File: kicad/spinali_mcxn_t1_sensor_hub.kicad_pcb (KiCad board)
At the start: 6 copper layers, 36.6 x 46 mm, 204 parts, among them J1 5055780421, J10 SDO, J11 CKO, J12 GND, J2 USB4105-GF-A, J3 CAN0A, J4 CAN0B, J5 Debug, J6 CAN1A, J7 CAN1B, J8 DF40TC(3.0)-50DP-0.4V(51), J9 DF40TC(3.0)-50DP-0.4V(51), Q1 BUK6D56-60EX, SW1 SW_SPST, U1 LM74700, U10 BMM350, U11 BMP581, U12 TJA1462ATK, U13 TJA1462ATK, U14 SK9822-EC20, U15 TJA1103AHN, U2 NX5P3363UKZ, U3 LM5160DNTJ, U4 NX5P3363UKZ, U5 MIC5504-1.8YMT, U6 MPM3811GG-Z, U7 MCXN947VDFT, U8 PCMF1USB3SZ, U9 ICM-45686, Y1 24MHz, Y2 32.768kHz, Y3 25MHz

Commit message: Updated layout
Added formal board-name in silkscreen.
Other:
- board text added: "X-MR-MCXN-T1"
- board text removed: "MR-XXX-XXX"
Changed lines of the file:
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@@
 		)
 	)
-	(gr_text "MR-XXX-XXX"
+	(gr_text "X-MR-MCXN-T1"
 		(at 118.2 100.5 90)
 		(layer "B.SilkS")

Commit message: Updated layout
Made edge cut dimensions easy to work with values.
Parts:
- moved J2 0.06 mm to (85.9, 100.7)
- moved U8 0.05 mm to (91.4, 100.2)
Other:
- board size 36.6 x 46 mm -> 36.5 x 46 mm
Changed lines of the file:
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@@
 	(footprint "TVS:PESD1USB3BCX"
 		(layer "B.Cu")
-		(at 91.35 100.2 -90)
+		(at 91.4 100.2 -90)
 		(descr "WLCSP5_2-1-2")
 		(tags "Diode")
@@
 	(footprint "Connector_USB:USB_C_Receptacle_GCT_USB4105-xx-A_16P_TopMnt_Horizontal"
 		(layer "B.Cu")
-		(at 85.85 100.7 90)
+		(at 85.91 100.7 90)
 		(descr "USB 2.0 Type C Receptacle, GCT, 16P, top mounted, horizontal, 5A: https://gct.co/files/drawings/usb4105.pdf")
 		(tags "USB C Type-C Receptacle SMD USB 2.0 16P 16C USB4105-15-A USB4105-15-A-060 USB4105-15-A-120 USB4105-GF-A USB4105-GF-A-060 USB4105-GF-A-120")
@@
 	)
 	(gr_rect
-		(start 82.15 75.95)
-		(end 118.75 122)
+		(start 82.2 75.95)
+		(end 118.7 121.95)
 		(stroke
 			(width 0.05)
@@
 	)
 	(via
-		(at 91.35 99.8)
+		(at 91.4 99.8)
 		(size 0.3)
 		(drill 0.2)
@@
 	)
 	(via
-		(at 91.35 100.6)
+		(at 91.4 100.6)
 		(size 0.3)
 		(drill 0.2)
@@
 	)
 	(segment
-		(start 91.35 100.2)
-		(end 91.35 99.85)
+		(start 91.4 100.2)
+		(end 91.4 99.85)
 		(width 0.16)
 		(layer "B.Cu")
@@
 	)
 	(segment
-		(start 91.35 99.85)
-		(end 91.35 99.8)
+		(start 91.4 99.85)
+		(end 91.4 99.8)
 		(width 0.16)
 		(layer "B.Cu")
@@
 	)
 	(segment
-		(start 91.35 100.55)
-		(end 91.35 100.6)
+		(start 91.4 100.55)
+		(end 91.4 100.6)
 		(width 0.16)
 		(layer "B.Cu")
@@
 	)
 	(segment
-		(start 91.35 100.2)
-		(end 91.35 100.55)
+		(start 91.4 100.2)
+		(end 91.4 100.55)
 		(width 0.16)
 		(layer "B.Cu")
@@
 	)
 	(segment
-		(start 88.55 102.730406)
-		(end 88.922297 103.102703)
+		(start 89.59 98.3)
+		(end 88.979594 98.3)
 		(width 0.3)
 		(layer "B.Cu")
@@
 	)
 	(segment
-		(start 89.527297 103.102703)
-		(end 89.53 103.1)
-		(width 0.3)
+		(start 88.025 102.205406)
+		(end 88.025 99.230001)
+		(width 0.5)
 		(layer "B.Cu")
 		(net 22)
 	)
 	(segment
-		(start 88.955001 98.3)
-		(end 88.630001 98.625)
+		(start 88.979594 103.1)
+		(end 89.53 103.1)
 		(width 0.3)
 		(layer "B.Cu")
@@
 	)
 	(segment
-		(start 88.922297 103.102703)
-		(end 89.527297 103.102703)
+		(start 88.61 102.730406)
+		(end 88.979594 103.1)
 		(width 0.3)
 		(layer "B.Cu")
@@
 	)
 	(segment
-		(start 89.53 98.3)
+		(start 89.59 98.3)
 		(end 90.4 98.3)
 		(width 0.5)
@@
 	)
 	(segment
-		(start 88.025 102.205406)
-		(end 88.025 99.230001)
+		(start 88.55 102.730406)
+		(end 88.61 102.730406)
+		(width 0.3)
+		(layer "B.Cu")
+		(net 22)
+	)
+	(segment
+		(start 88.025 99.230001)
+		(end 88.630001 98.625)
 		(width 0.5)
 		(layer "B.Cu")
@@
 	)
 	(segment
-		(start 88.025 99.230001)
+		(start 88.654594 98.625)
 		(end 88.630001 98.625)
-		(width 0.5)
+		(width 0.3)
 		(layer "B.Cu")
 		(net 22)
 	)
 	(segment
-		(start 89.53 98.3)
-		(end 88.955001 98.3)
+		(start 88.979594 98.3)
+		(end 88.654594 98.625)
 		(width 0.3)
 		(layer "B.Cu")
@@
 	)
 	(segment
-		(start 87.67 96.38)
-		(end 88.955 96.38)
-		(width 0.1)
-		(layer "F.Cu")
-		(net 24)
-	)
-	(segment
-		(start 83.605 105.02)
-		(end 83.6 105.025)
-		(width 0.1)
-		(layer "F.Cu")
-		(net 24)
-	)
-	(segment
 		(start 83.47 101.175)
 		(end 83.47 100.695)
@@
 	)
 	(segment
-		(start 84.775 105.02)
-		(end 83.605 105.02)
+		(start 87.7 96.38)
+		(end 88.955 96.38)
 		(width 0.1)
 		(layer "F.Cu")
@@
 	)
 	(segment
-		(start 87.65 96.4)
-		(end 87.67 96.38)
+		(start 83.47 100.695)
+		(end 83.45 100.675)
 		(width 0.1)
 		(layer "F.Cu")
@@
 	)
 	(segment
-		(start 83.47 100.695)
+		(start 83.44 100.665)
 		(end 83.45 100.675)
 		(width 0.1)
@@
 	)
 	(segment
-		(start 83.44 100.665)
-		(end 83.45 100.675)
+		(start 83.7 96.38)
+		(end 84.775 96.38)
 		(width 0.1)
 		(layer "F.Cu")
@@
 	)
 	(segment
-		(start 83.62 96.38)
-		(end 84.775 96.38)
+		(start 83.65 105.02)
+		(end 84.775 105.02)
 		(width 0.1)
 		(layer "F.Cu")
@@
 	)
 	(segment
-		(start 87.63 105.02)
+		(start 87.7 105.02)
 		(end 88.955 105.02)
 		(width 0.1)
@@
 	)
 	(via
-		(at 83.62 96.38)
+		(at 83.7 96.38)
 		(size 0.3)
 		(drill 0.2)
@@
 	)
 	(via
-		(at 87.63 105.02)
+		(at 87.7 105.02)
 		(size 0.3)
 		(drill 0.2)
@@
 	)
 	(via
-		(at 83.6 105.025)
+		(at 83.65 105.02)
 		(size 0.3)
 		(drill 0.2)
@@
 	)
 	(via
-		(at 87.65 96.4)
+		(at 87.7 96.38)
 		(size 0.3)
 		(drill 0.2)
@@
 	)
 	(segment
-		(start 89.53 100.95)
-		(end 88.89 100.95)
-		(width 0.16)
-		(layer "B.Cu")
-		(net 231)
-	)
-	(segment
-		(start 89.53 99.95)
-		(end 89.58 100)
+		(start 88.63 100.21)
+		(end 88.89 99.95)
 		(width 0.16)
 		(layer "B.Cu")
@@
 	)
 	(segment
-		(start 88.63 100.69)
-		(end 88.63 100.21)
+		(start 89.53 100.95)
+		(end 88.89 100.95)
 		(width 0.16)
 		(layer "B.Cu")
@@
 	)
 	(segment
-		(start 88.63 100.21)
-		(end 88.89 99.95)
+		(start 89.58 100)
+		(end 91 100)
 		(width 0.16)
 		(layer "B.Cu")
@@
 	)
 	(segment
-		(start 88.89 99.95)
-		(end 89.53 99.95)
+		(start 88.63 100.69)
+		(end 88.63 100.21)
 		(width 0.16)
 		(layer "B.Cu")
@@
 	)
 	(segment
-		(start 89.58 100)
-		(end 90.95 100)
+		(start 89.53 99.95)
+		(end 89.58 100)
 		(width 0.16)
 		(layer "B.Cu")
@@
 	)
 	(segment
-		(start 90.17 101.45)
-		(end 90.44 101.18)
-		(width 0.16)
-		(layer "B.Cu")
-		(net 232)
-	)
-	(segment
-		(start 90.44 101.18)
-		(end 90.44 100.41)
+		(start 88.89 99.95)
+		(end 89.53 99.95)
 		(width 0.16)
 		(layer "B.Cu")
-		(net 232)
+		(net 231)
 	)
 	(segment
-		(start 90.36 100.41)
-		(end 90.916532 100.41)
+		(start 89.53 100.45)
+		(end 89.57 100.41)
 		(width 0.16)
 		(layer "B.Cu")
@@
 	)
 	(segment
-		(start 89.57 100.41)
-		(end 90.36 100.41)
+		(start 90.17 101.45)
+		(end 90.44 101.18)
 		(width 0.16)
 		(layer "B.Cu")
@@
 	)
 	(segment
-		(start 90.916532 100.41)
-		(end 90.928266 100.421734)
+		(start 89.57 100.41)
+		(end 90.99 100.41)
 		(width 0.16)
 		(layer "B.Cu")
@@
 	)
 	(segment
-		(start 89.53 100.45)
-		(end 89.57 100.41)
+		(start 90.44 101.18)
+		(end 90.44 100.41)
 		(width 0.16)
 		(layer "B.Cu")
@@
 	)
 	(segment
-		(start 92.45 100.4)
-		(end 91.75 100.4)
+		(start 92.6 100.55)
+		(end 92.45 100.4)
 		(width 0.16)
 		(layer "B.Cu")
@@
 	)
 	(segment
-		(start 92.6 100.55)
-		(end 92.45 100.4)
+		(start 92.45 100.4)
+		(end 91.8 100.4)
 		(width 0.16)
 		(layer "B.Cu")
@@
 	(segment
 		(start 92.6764 99.99)
-		(end 91.76 99.99)
+		(end 91.81 99.99)
 		(width 0.16)
 		(layer "B.Cu")
@@
 	)
 	(segment
-		(start 92.9182 100.2318)
-		(end 92.6764 99.99)
+		(start 91.81 99.99)
+		(end 91.8 100)
 		(width 0.16)
 		(layer "B.Cu")
@@
 	)
 	(segment
-		(start 91.76 99.99)
-		(end 91.75 100)
+		(start 92.9182 100.2318)
+		(end 92.6764 99.99)
 		(width 0.16)
 		(layer "B.Cu")

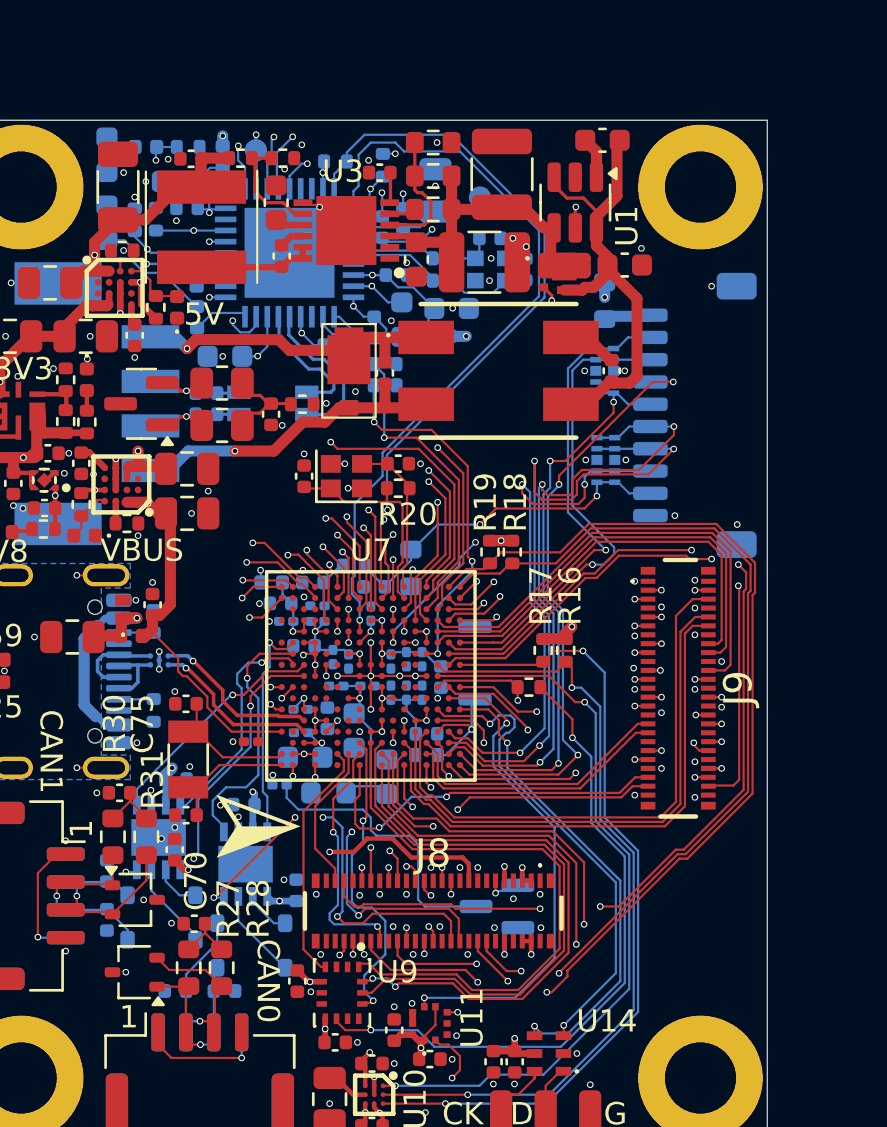
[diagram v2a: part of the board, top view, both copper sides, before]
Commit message: Update layout
- Length matched MII RX and TX.
- Made clearance between USB D+ and D- traces constant.
- Improved traces for 32kHz crystal.
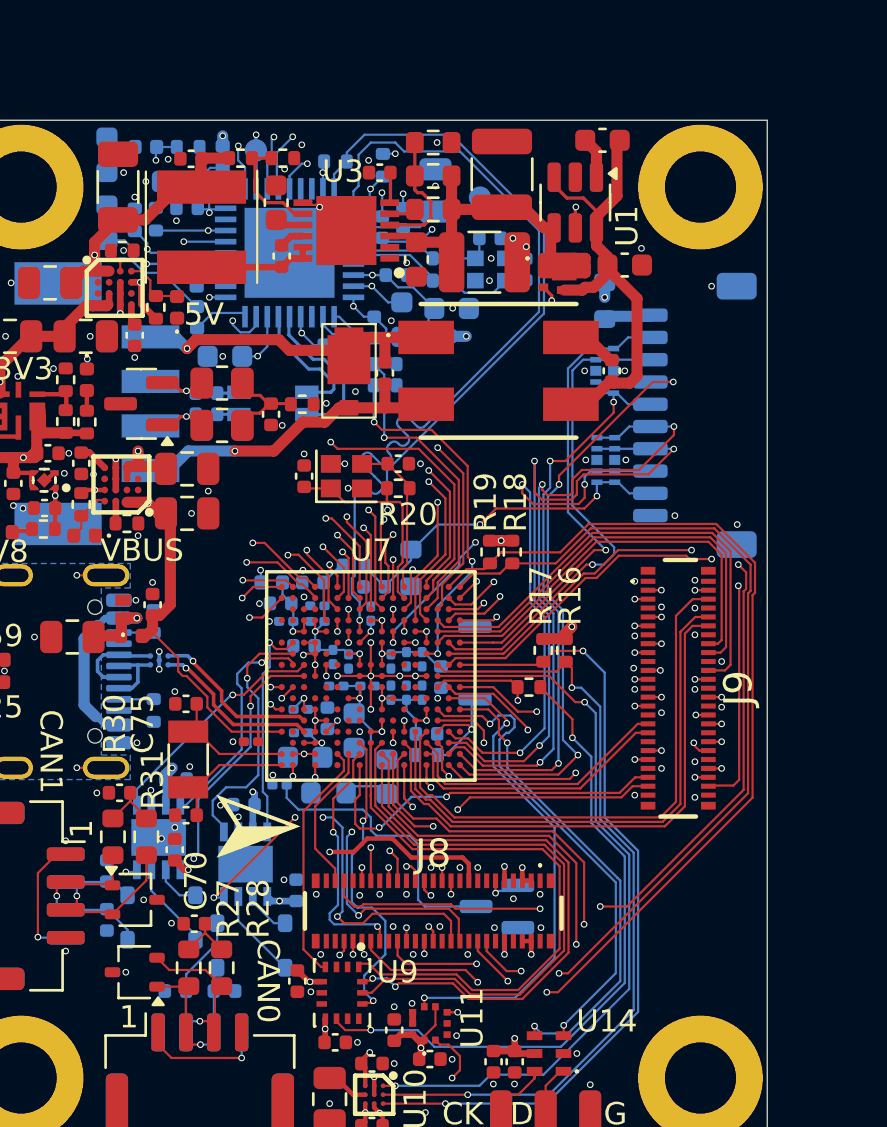
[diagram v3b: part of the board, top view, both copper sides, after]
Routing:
- net P1_7/ENET0_TXD1: track 24.6 -> 29.8 mm
- net P1_20/ENET0_MDC: track 34.1 -> 39.1 mm
- net P1_14/ENET0_RXD0: track 24.1 -> 28.0 mm
- net P1_13/ENET0_RXDV: track 26.0 -> 25.4 mm
